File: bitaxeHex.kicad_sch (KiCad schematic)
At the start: 25 parts, among them J1 XT30

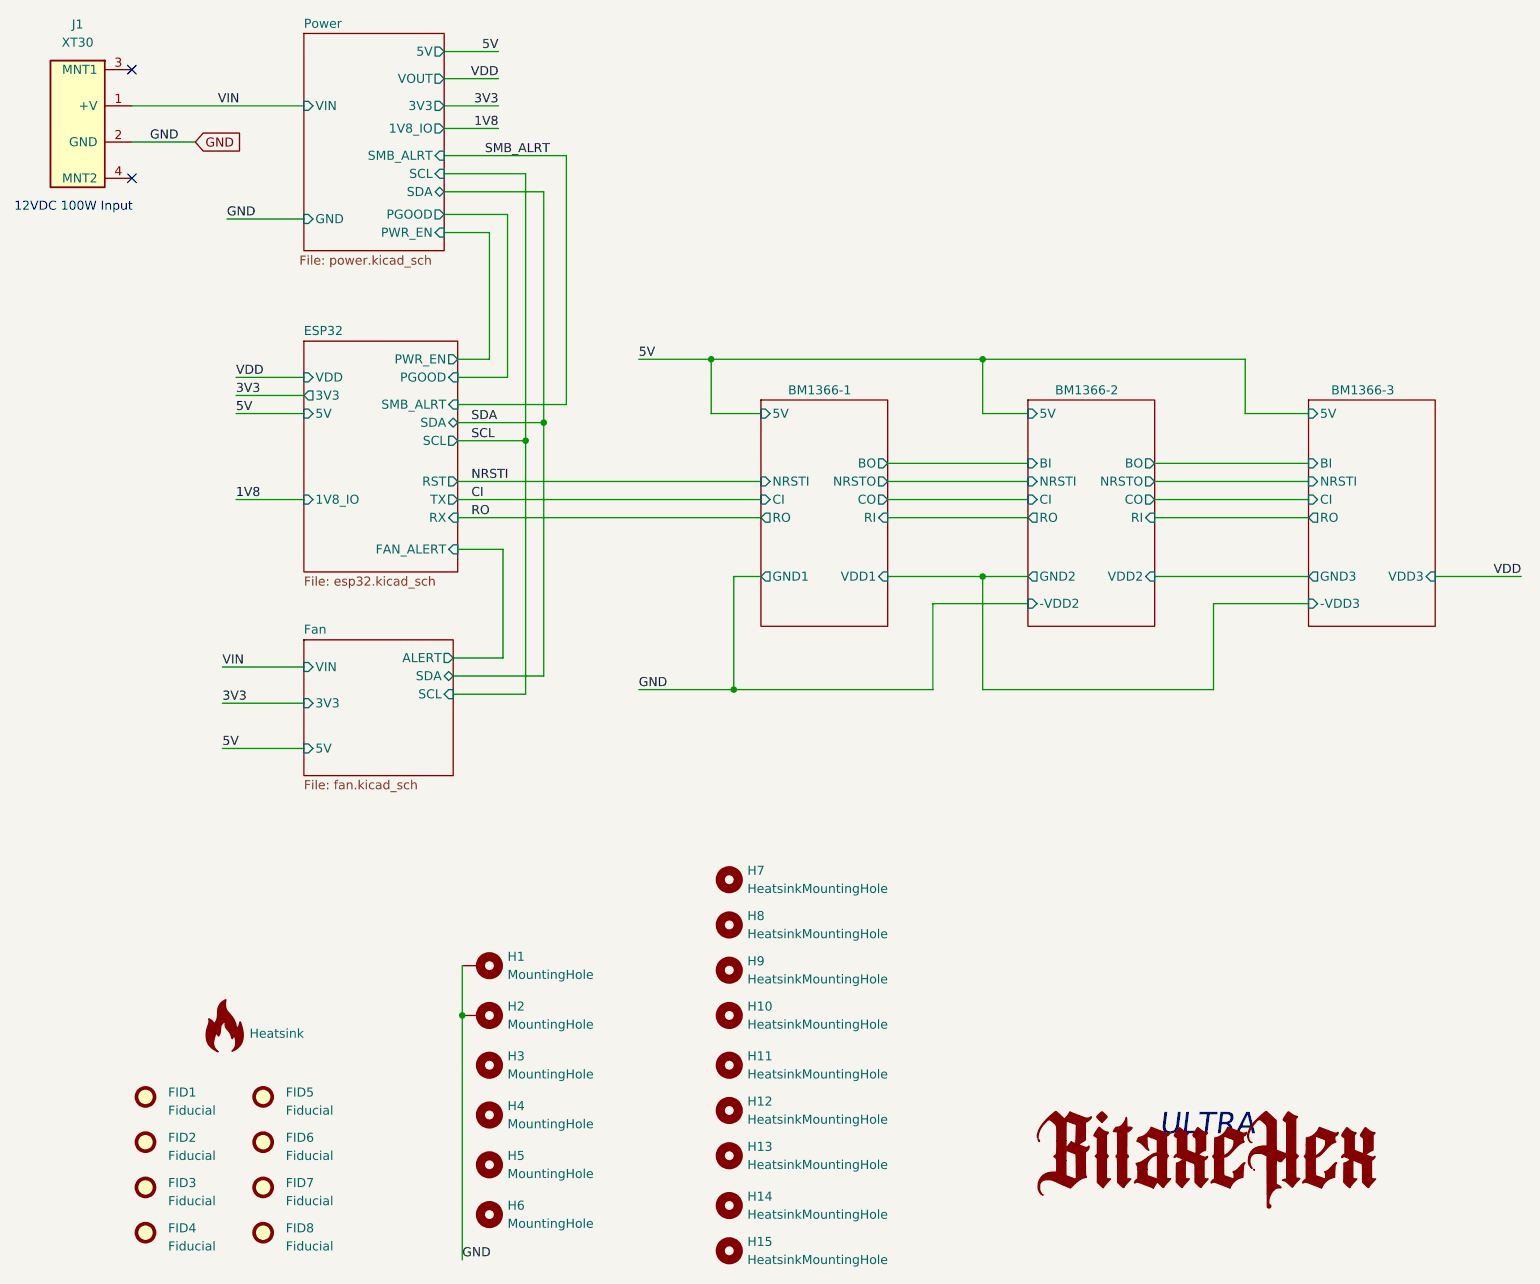
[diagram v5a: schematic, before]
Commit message: fix OP-AMP power supply, connect to GND,+5V
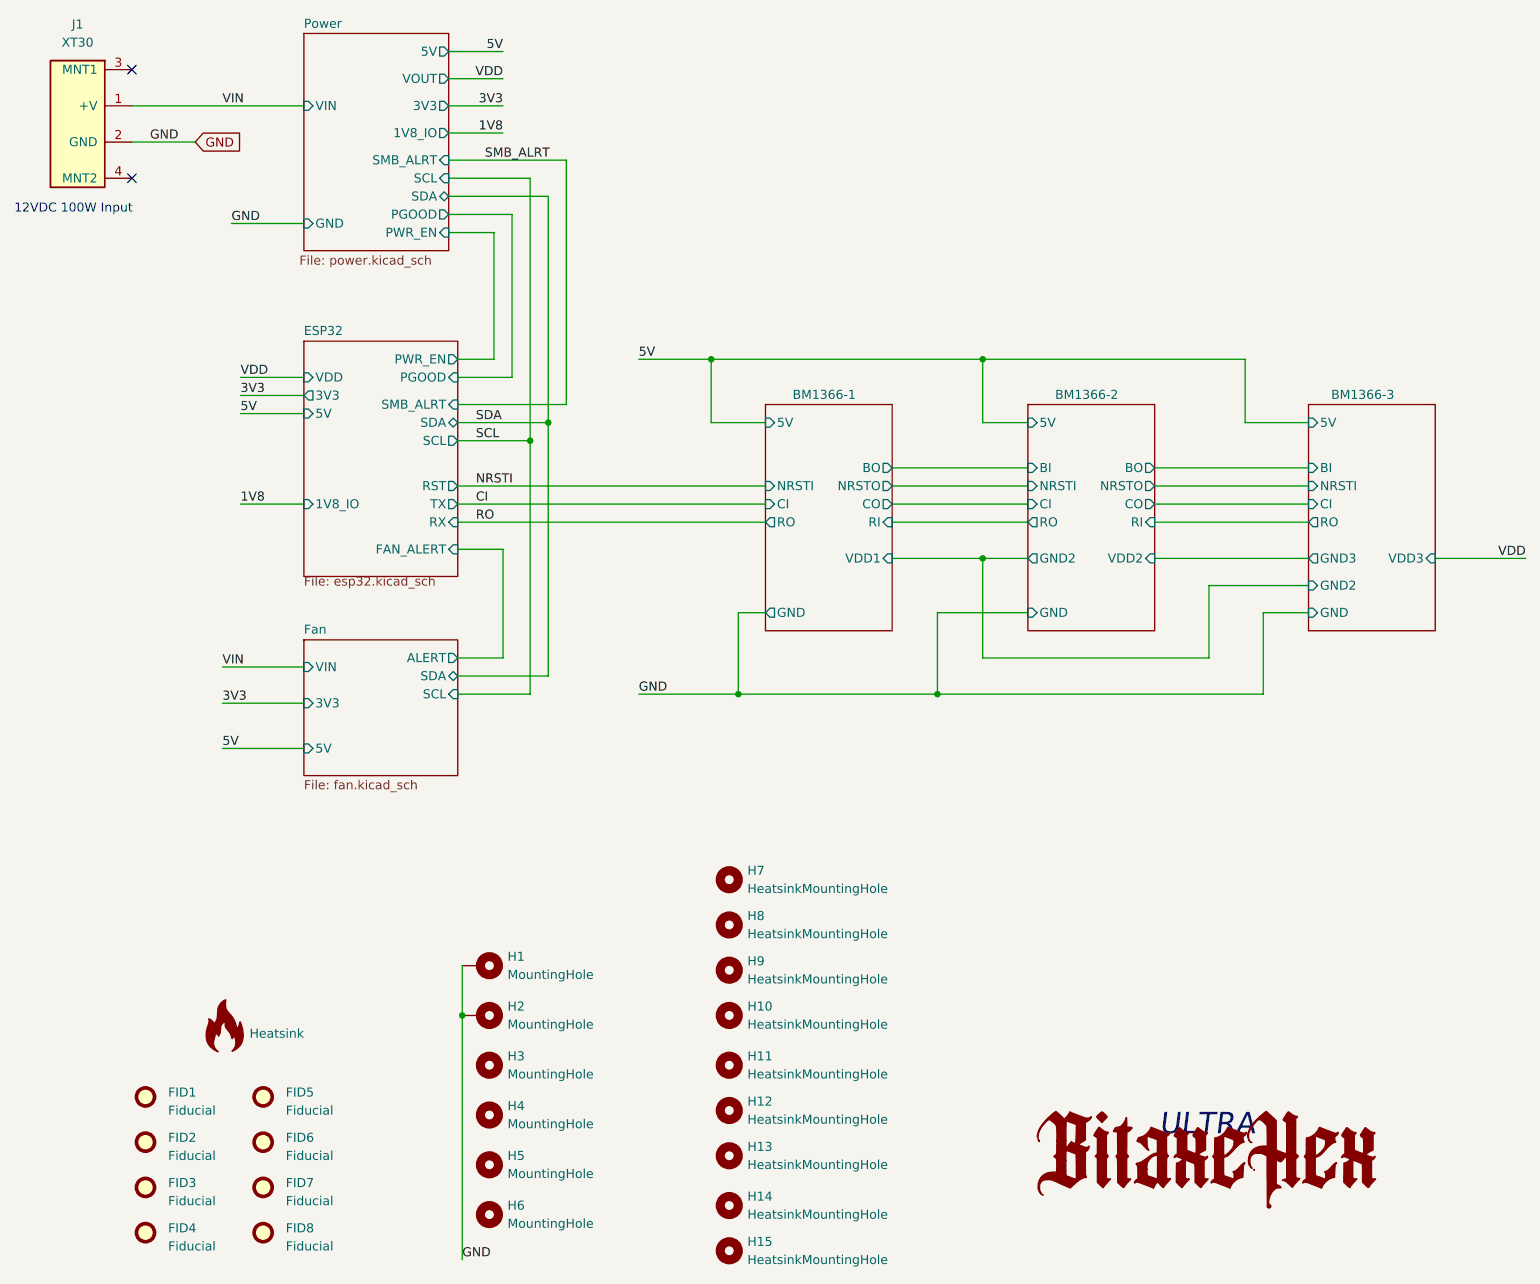
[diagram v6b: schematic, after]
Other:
- sheet BM1366-1 ports: added GND; removed GND1
- sheet BM1366-2 ports: added GND; removed -VDD2
- sheet BM1366-3 ports: added GND, GND2; removed -VDD3

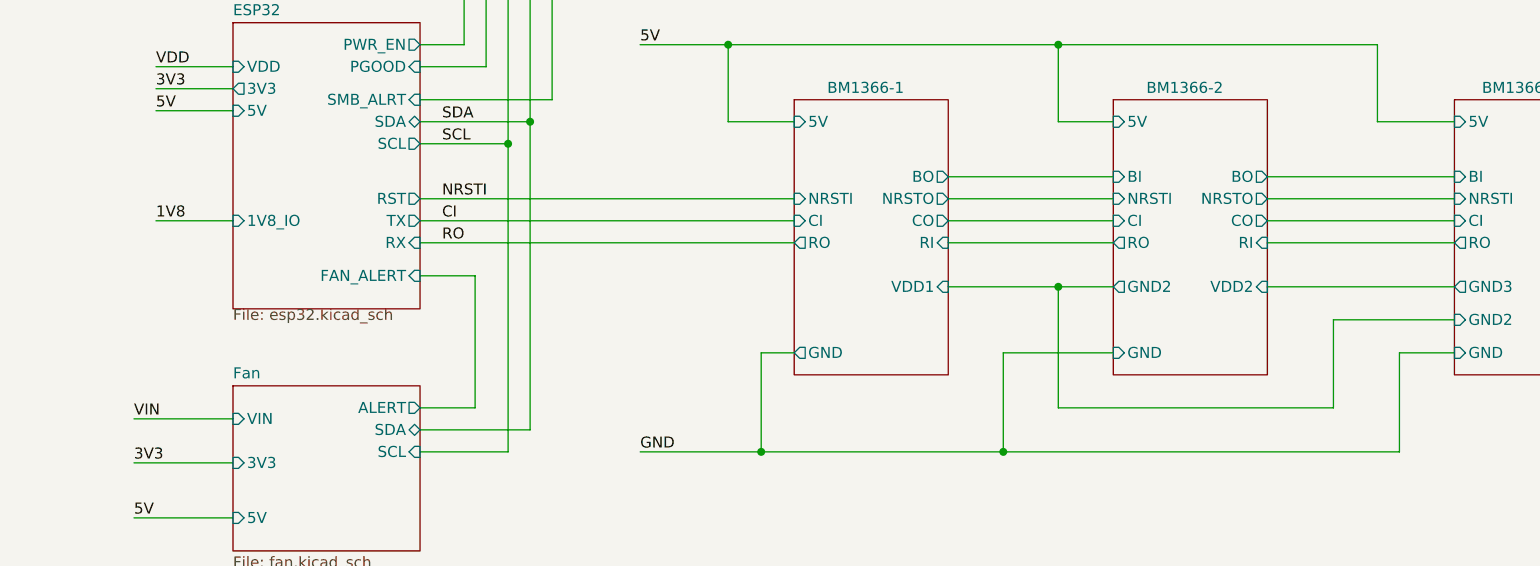
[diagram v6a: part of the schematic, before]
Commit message: add voltage domain sense signals to the ESP32 ADC
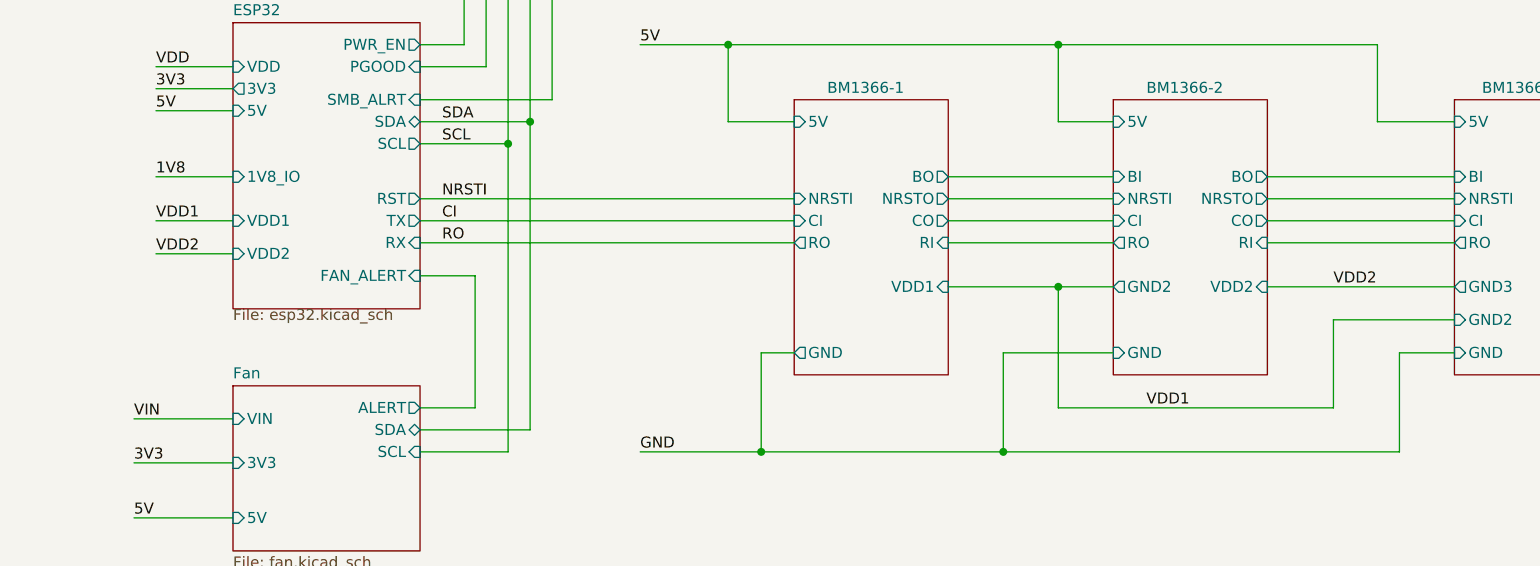
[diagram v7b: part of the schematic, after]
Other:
- sheet ESP32 ports: added VDD1, VDD2; removed none
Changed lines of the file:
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@@
 	(wire
 		(pts
-			(xy 50.8 88.9) (xy 59.69 88.9)
+			(xy 154.94 68.58) (xy 191.77 68.58)
 		)
 		(stroke
@@
 	(wire
 		(pts
-			(xy 154.94 68.58) (xy 191.77 68.58)
+			(xy 50.8 92.71) (xy 59.69 92.71)
 		)
 		(stroke
@@
 	(wire
 		(pts
+			(xy 50.8 83.82) (xy 59.69 83.82)
+		)
+		(stroke
+			(width 0)
+			(type default)
+		)
+	)
+	(wire
+		(pts
 			(xy 96.52 74.93) (xy 96.52 40.64)
 		)
@@
 	(wire
 		(pts
+			(xy 50.8 88.9) (xy 59.69 88.9)
+		)
+		(stroke
+			(width 0)
+			(type default)
+		)
+	)
+	(wire
+		(pts
 			(xy 142.24 88.9) (xy 161.29 88.9)
 		)
@@
 	)
 	(label "1V8"
-		(at 50.8 88.9 0)
+		(at 50.8 83.82 0)
 		(fields_autoplaced yes)
 		(effects
@@
 		)
 	)
+	(label "VDD1"
+		(at 165.1 110.49 0)
+		(fields_autoplaced yes)
+		(effects
+			(font
+				(size 1.27 1.27)
+			)
+			(justify left bottom)
+		)
+	)
+	(label "VDD1"
+		(at 50.8 88.9 0)
+		(fields_autoplaced yes)
+		(effects
+			(font
+				(size 1.27 1.27)
+			)
+			(justify left bottom)
+		)
+	)
 	(label "5V"
 		(at 106.68 68.58 0)
@@
 		)
 	)
+	(label "VDD2"
+		(at 50.8 92.71 0)
+		(fields_autoplaced yes)
+		(effects
+			(font
+				(size 1.27 1.27)
+			)
+			(justify left bottom)
+		)
+	)
 	(label "NRSTI"
 		(at 83.82 86.36 0)
@@
 		)
 	)
+	(label "VDD2"
+		(at 186.69 96.52 0)
+		(fields_autoplaced yes)
+		(effects
+			(font
+				(size 1.27 1.27)
+			)
+			(justify left bottom)
+		)
+	)
 	(label "RO"
 		(at 83.82 91.44 0)
@@
 		)
 		(pin "1V8_IO" input
-			(at 59.69 88.9 180)
+			(at 59.69 83.82 180)
 			(effects
 				(font
@@
 			)
 		)
+		(pin "VDD1" input
+			(at 59.69 88.9 180)
+			(effects
+				(font
+					(size 1.27 1.27)
+				)
+				(justify left)
+			)
+		)
+		(pin "VDD2" input
+			(at 59.69 92.71 180)
+			(effects
+				(font
+					(size 1.27 1.27)
+				)
+				(justify left)
+			)
+		)

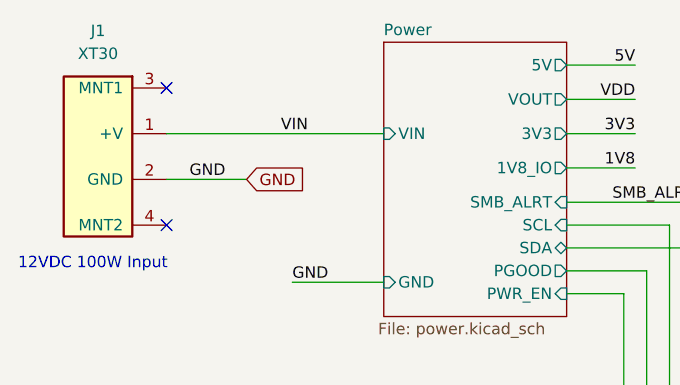
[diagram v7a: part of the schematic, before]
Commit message: add XT30 3D model
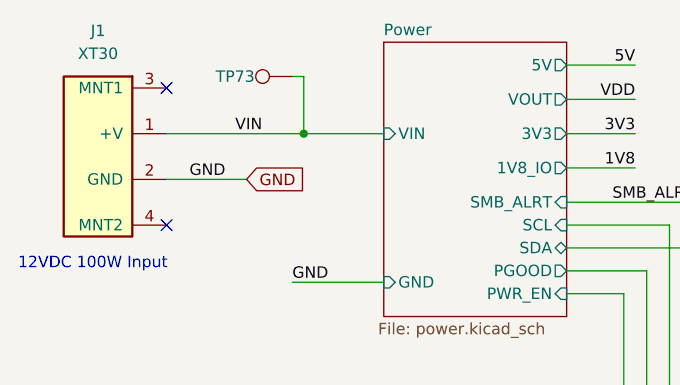
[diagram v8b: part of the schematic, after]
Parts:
- added TP73: TestPoint, TestPoint:TestPoint_Pad_D1.0mm, symbol Connector:TestPoint
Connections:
- net VIN: now also TP73.1
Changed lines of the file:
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@@
+	)
+	(junction
+		(at 50.8 33.02)
+		(diameter 0)
+		(color 0 0 0 0)
 	)
 	(junction
@@
 	(wire
 		(pts
+			(xy 49.53 26.67) (xy 50.8 26.67)
+		)
+		(stroke
+			(width 0)
+			(type default)
+		)
+	)
+	(wire
+		(pts
 			(xy 81.28 74.93) (xy 96.52 74.93)
 		)
@@
 	(wire
 		(pts
+			(xy 50.8 26.67) (xy 50.8 33.02)
+		)
+		(stroke
+			(width 0)
+			(type default)
+		)
+	)
+	(wire
+		(pts
 			(xy 200.66 77.47) (xy 191.77 77.47)
 		)
@@
 	(wire
 		(pts
+			(xy 35.56 33.02) (xy 50.8 33.02)
+		)
+		(stroke
+			(width 0)
+			(type default)
+		)
+	)
+	(wire
+		(pts
 			(xy 48.26 111.76) (xy 59.69 111.76)
 		)
@@
 	(wire
 		(pts
-			(xy 35.56 33.02) (xy 59.69 33.02)
-		)
-		(stroke
-			(width 0)
-			(type default)
-		)
-	)
-	(wire
-		(pts
 			(xy 218.44 96.52) (xy 231.14 96.52)
 		)
@@
 		(pts
 			(xy 124.46 86.36) (xy 81.28 86.36)
+		)
+		(stroke
+			(width 0)
+			(type default)
+		)
+	)
+	(wire
+		(pts
+			(xy 50.8 33.02) (xy 59.69 33.02)
 		)
 		(stroke
@@
 	)
 	(label "VIN"
-		(at 48.26 33.02 0)
+		(at 43.18 33.02 0)
 		(fields_autoplaced yes)
 		(effects
@@
 					(unit 1)
 				)
+			)
+		)
+	)
+	(symbol
+		(lib_id "Connector:TestPoint")
+		(at 49.53 26.67 90)
+		(mirror x)
+		(unit 1)
+		(exclude_from_sim no)
+		(in_bom no)
+		(on_board yes)
+		(dnp no)
+		(property "Reference" "TP73"
+			(at 43.18 26.67 90)
+			(effects
+				(font
+					(size 1.27 1.27)
+				)
+			)
+		)
+		(property "Value" "TestPoint"
+			(at 43.815 27.9399 90)
+			(effects
+				(font
+					(size 1.27 1.27)
+				)
+				(justify left)
+				(hide yes)
+			)
+		)
+		(property "Footprint" "TestPoint:TestPoint_Pad_D1.0mm"
+			(at 49.53 31.75 0)
+			(effects
+				(font
+					(size 1.27 1.27)
+				)
+				(hide yes)
+			)
+		)
+		(property "Datasheet" "~"
+			(at 49.53 31.75 0)
+			(effects
+				(font
+					(size 1.27 1.27)
+				)
+				(hide yes)
+			)
+		)
+		(property "Description" ""
+			(at 49.53 26.67 0)
+			(effects
+				(font
+					(size 1.27 1.27)
+				)
+				(hide yes)
+			)
+		)
+		(pin "1"
+		)
+		(instances
+			(project "bitaxeHex"
+				(path "/e63e39d7-6ac0-4ffd-8aa3-1841a4541b55"
+					(reference "TP73")
+					(unit 1)
+				)
